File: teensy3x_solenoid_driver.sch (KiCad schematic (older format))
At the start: 43 parts, among them J1 Conn_01x02, J10 Jack-DC, J2 Conn_01x02, J3 Conn_01x02, J4 Conn_01x02, J5 Conn_01x02, J6 Conn_01x02, J7 Conn_01x02, J8 Conn_01x02, J9 Conn_02x05_Odd_Even, Q1 NPN_Darlington, Q2 NPN_Darlington, Q3 NPN_Darlington, Q4 NPN_Darlington, Q5 NPN_Darlington, Q6 NPN_Darlington, Q7 NPN_Darlington, Q8 NPN_Darlington, U1 TEENSY3x

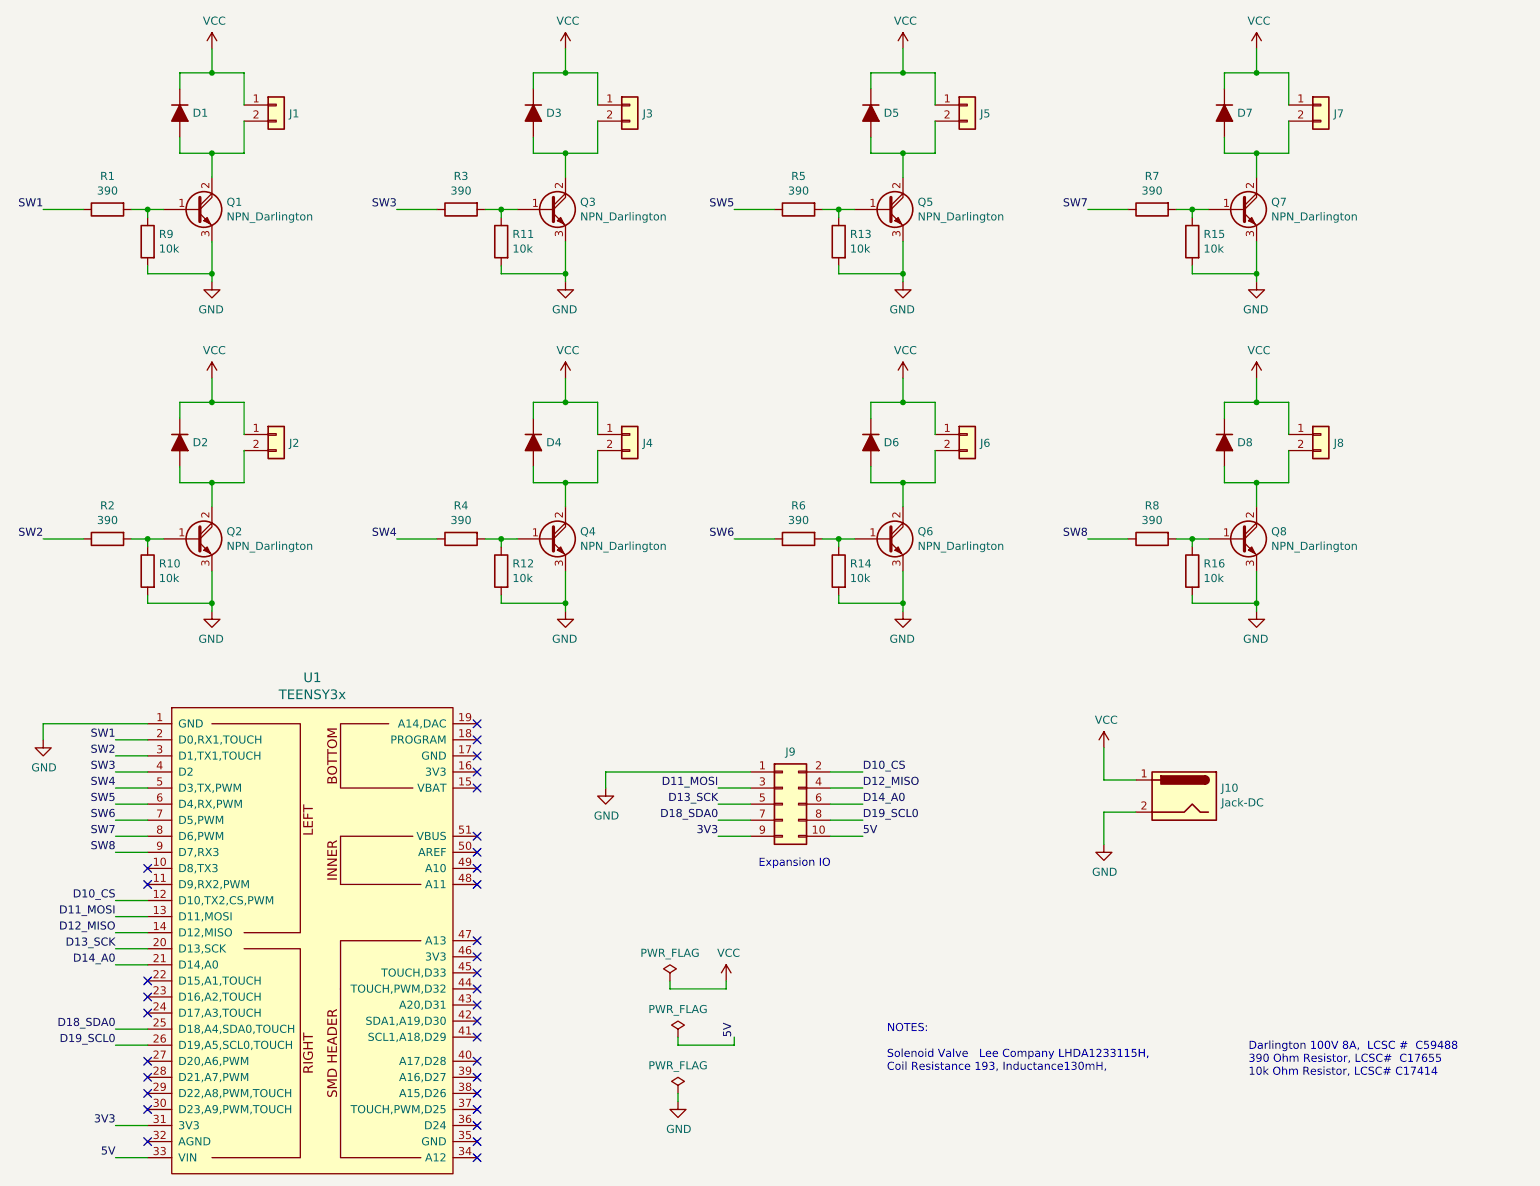
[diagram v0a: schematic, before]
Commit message: Changed base resistor ... forgot about extra voltage drop due to darlington transistor.
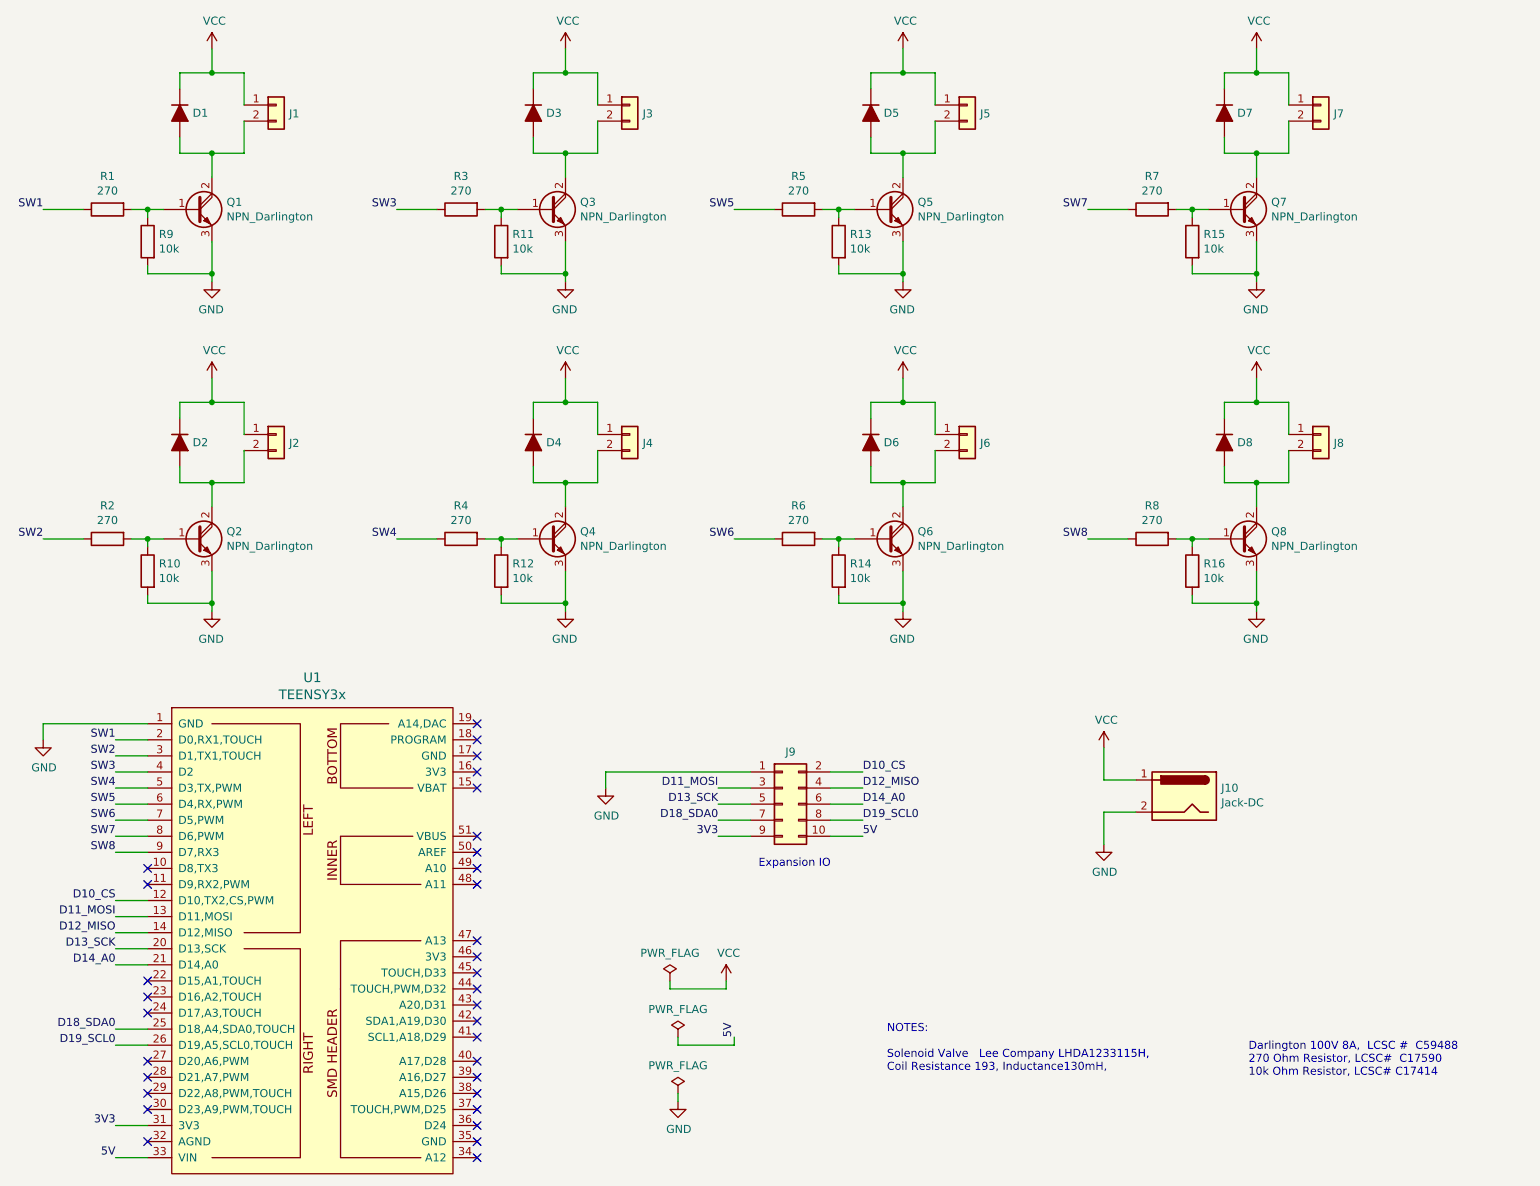
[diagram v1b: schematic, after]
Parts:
- R1, R2, R3, R4, R5, R6, R7, R8: value 390 -> 270
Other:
- note added: "Darlington 100V 8A, LCSC # C59488 \n270 Ohm Resistor, LCSC# C17590\n10k Ohm Resistor, LCSC# C17414"
- note removed: "Darlington 100V 8A, LCSC # C59488 \n390 Ohm Resistor, LCSC# C17655\n10k Ohm Resistor, LCSC# C17414"
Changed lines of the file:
@@
 P 1600 1750
 F 0 "R1" V 1393 1750 50  0000 C CNN
-F 1 "390" V 1484 1750 50  0000 C CNN
+F 1 "270" V 1484 1750 50  0000 C CNN
 F 2 "" V 1530 1750 50  0001 C CNN
 F 3 "~" H 1600 1750 50  0001 C CNN
@@
 P 3800 1750
 F 0 "R3" V 3593 1750 50  0000 C CNN
-F 1 "390" V 3684 1750 50  0000 C CNN
+F 1 "270" V 3684 1750 50  0000 C CNN
 F 2 "" V 3730 1750 50  0001 C CNN
 F 3 "~" H 3800 1750 50  0001 C CNN
@@
 P 5900 1750
 F 0 "R5" V 5693 1750 50  0000 C CNN
-F 1 "390" V 5784 1750 50  0000 C CNN
+F 1 "270" V 5784 1750 50  0000 C CNN
 F 2 "" V 5830 1750 50  0001 C CNN
 F 3 "~" H 5900 1750 50  0001 C CNN
@@
 P 8100 1750
 F 0 "R7" V 7893 1750 50  0000 C CNN
-F 1 "390" V 7984 1750 50  0000 C CNN
+F 1 "270" V 7984 1750 50  0000 C CNN
 F 2 "" V 8030 1750 50  0001 C CNN
 F 3 "~" H 8100 1750 50  0001 C CNN
@@
 P 1600 3800
 F 0 "R2" V 1393 3800 50  0000 C CNN
-F 1 "390" V 1484 3800 50  0000 C CNN
+F 1 "270" V 1484 3800 50  0000 C CNN
 F 2 "" V 1530 3800 50  0001 C CNN
 F 3 "~" H 1600 3800 50  0001 C CNN
@@
 P 3800 3800
 F 0 "R4" V 3593 3800 50  0000 C CNN
-F 1 "390" V 3684 3800 50  0000 C CNN
+F 1 "270" V 3684 3800 50  0000 C CNN
 F 2 "" V 3730 3800 50  0001 C CNN
 F 3 "~" H 3800 3800 50  0001 C CNN
@@
 P 5900 3800
 F 0 "R6" V 5693 3800 50  0000 C CNN
-F 1 "390" V 5784 3800 50  0000 C CNN
+F 1 "270" V 5784 3800 50  0000 C CNN
 F 2 "" V 5830 3800 50  0001 C CNN
 F 3 "~" H 5900 3800 50  0001 C CNN
@@
 P 8100 3800
 F 0 "R8" V 7893 3800 50  0000 C CNN
-F 1 "390" V 7984 3800 50  0000 C CNN
+F 1 "270" V 7984 3800 50  0000 C CNN
 F 2 "" V 8030 3800 50  0001 C CNN
 F 3 "~" H 8100 3800 50  0001 C CNN
@@
 $EndComp
 Text Notes 8700 7150 0    50   ~ 0
-Darlington 100V 8A,  LCSC #  C59488  \n390 Ohm Resistor, LCSC#  C17655\n10k Ohm Resistor, LCSC# C17414
+Darlington 100V 8A,  LCSC #  C59488  \n270 Ohm Resistor, LCSC#  C17590\n10k Ohm Resistor, LCSC# C17414
 Wire Wire Line
 	8000 5300 7800 5300
